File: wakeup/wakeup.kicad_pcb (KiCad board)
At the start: 2 copper layers, 12 parts, among them J1 Conn_01x03_Female, U1 74HC00, U2 74HC393

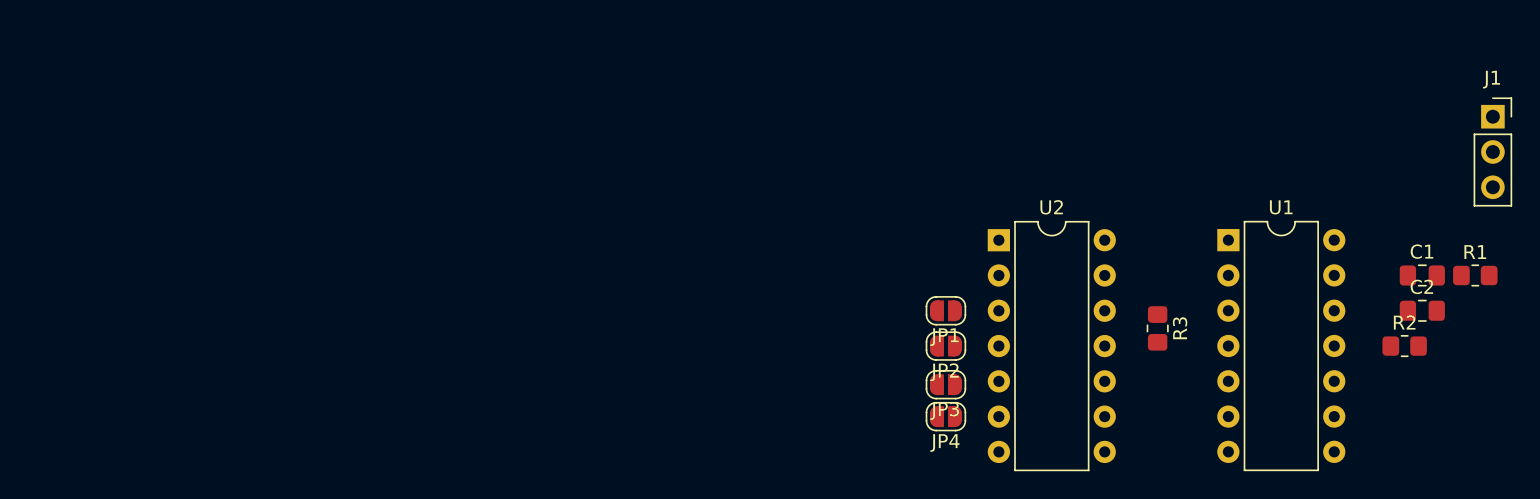
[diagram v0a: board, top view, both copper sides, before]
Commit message: Add power filter create pcb
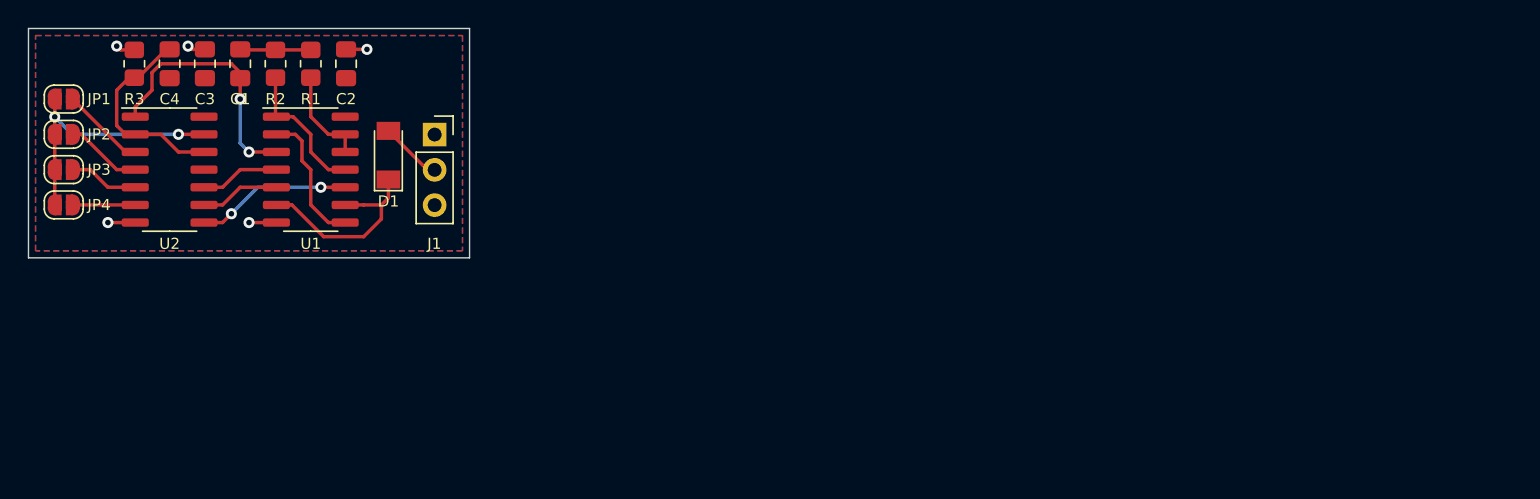
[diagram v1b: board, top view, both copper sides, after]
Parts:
- added C2: C, Capacitor_SMD:C_0805_2012Metric_Pad1.18x1.45mm_HandSolder, F.Cu at (48.3, 53.3)
- added C3: C, Capacitor_SMD:C_0805_2012Metric_Pad1.18x1.45mm_HandSolder, F.Cu at (38.1, 53.3)
- added D1: D, Diode_SMD:D_MiniMELF, F.Cu at (51.3, 59.9)
- U1, U2: footprint Package_DIP:DIP-14_W7.62mm -> Package_SO:SO-14_3.9x8.65mm_P1.27mm
- moved C4 91.9 mm to (35.6, 53.3), turned to 90 degrees
- moved C1 86.4 mm to (40.6, 53.3), turned to -90 degrees
- moved R1 85.2 mm to (45.7, 53.3), turned to -90 degrees
- moved R2 83.8 mm to (43.2, 53.3), turned to -90 degrees
- moved J1 76.2 mm to (54.6, 58.4)
- moved R3 76.1 mm to (33.0, 53.3), turned to 90 degrees
- moved U1 66.2 mm to (45.7, 61.0)
- moved JP3 65.4 mm to (27.9, 61.0)
- moved JP1 65.3 mm to (27.9, 55.9)
- moved JP2 65.3 mm to (27.9, 58.4)
- moved JP4 65.3 mm to (27.9, 63.5)
- moved U2 59.9 mm to (35.6, 61.0)
- renumbered C2 to C4
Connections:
- J1 pad 2: Net-(J1-Pad2) -> Net-(D1-Pad2)
- U1 pad 10: Net-(U1-Pad5) -> Net-(U1-Pad10)
- U1 pad 6: Net-(J1-Pad2) -> Net-(D1-Pad1)
- U1 pad 9: Net-(U2-Pad8) -> Net-(D1-Pad1)
- U2 pad 8: Net-(U2-Pad8) -> Net-(U1-Pad10)
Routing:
- net Net-(JP1-Pad2): track 0.00 -> 18.9 mm, vias 0 -> 2
- net Net-(C1-Pad2): track 0.00 -> 18.5 mm, vias 0 -> 2
- net Net-(D1-Pad1): track 0.00 -> 14.7 mm
- net Net-(C4-Pad2): track 0.00 -> 14.6 mm
- net Net-(U1-Pad10): track 0.00 -> 11.2 mm, vias 0 -> 2
- net Net-(R2-Pad2): track 0.00 -> 10.1 mm
- net Net-(U1-Pad2): track 0.00 -> 9.91 mm
- net GND: track 0.00 -> 8.14 mm, vias 0 -> 5
- net Net-(R1-Pad2): track 0.00 -> 7.08 mm
- net Net-(JP1-Pad1): track 0.00 -> 6.08 mm
- net Net-(U1-Pad5): track 0.00 -> 5.74 mm
- net Net-(U1-Pad4): track 0.00 -> 5.74 mm
- net Net-(JP2-Pad1): track 0.00 -> 5.55 mm
- net Net-(C1-Pad1): track 0.00 -> 5.10 mm
- net Net-(JP3-Pad1): track 0.00 -> 5.02 mm
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- added copper zone on B.Cu, net GND
- added copper zone on F.Cu, net VCC
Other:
- board outline added: 31.8 x 16.5 mm

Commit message: merge stage 1 update schematic ZX_keyboard
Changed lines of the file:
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@@
       (plotvalue true)
       (plotinvisibletext false)
-      (sketchpadsonfab false)
+      (sketchpadsonfab true)
       (subtractmaskfromsilk false)
       (outputformat 1)
       (mirror false)
-      (drillshape 1)
+      (drillshape 0)
       (scaleselection 1)
-      (outputdirectory "")
+      (outputdirectory "gerber/")
     )
   )
@@
     (fp_line (start -1 0.625) (end -1 -0.625) (layer "F.Fab") (width 0.1))
     (fp_line (start 1 -0.625) (end 1 0.625) (layer "F.Fab") (width 0.1))
-    (pad "1" smd roundrect (at -1.0375 0 90) (size 1.175 1.45) (layers "F.Cu" "F.Paste" "F.Mask") (roundrect_rratio 0.212766)
+    (pad "1" smd roundrect (at -1.0375 0 90) (size 1.175 1.45) (layers "F.Cu" "F.Paste" "F.Mask") (roundrect_rratio 0.2127659574)
       (net 3 "VCC") (pintype "passive"))
-    (pad "2" smd roundrect (at 1.0375 0 90) (size 1.175 1.45) (layers "F.Cu" "F.Paste" "F.Mask") (roundrect_rratio 0.212766)
+    (pad "2" smd roundrect (at 1.0375 0 90) (size 1.175 1.45) (layers "F.Cu" "F.Paste" "F.Mask") (roundrect_rratio 0.2127659574)
       (net 18 "Net-(C4-Pad2)") (pintype "passive"))
     (model "${KICAD6_3DMODEL_DIR}/Capacitor_SMD.3dshapes/C_0805_2012Metric.wrl"
@@
     (fp_line (start -1 0.625) (end -1 -0.625) (layer "F.Fab") (width 0.1))
     (fp_line (start 1 -0.625) (end 1 0.625) (layer "F.Fab") (width 0.1))
-    (pad "1" smd roundrect (at -1.0375 0 90) (size 1.175 1.45) (layers "F.Cu" "F.Paste" "F.Mask") (roundrect_rratio 0.212766)
+    (pad "1" smd roundrect (at -1.0375 0 90) (size 1.175 1.45) (layers "F.Cu" "F.Paste" "F.Mask") (roundrect_rratio 0.2127659574)
       (net 3 "VCC") (pintype "passive"))
-    (pad "2" smd roundrect (at 1.0375 0 90) (size 1.175 1.45) (layers "F.Cu" "F.Paste" "F.Mask") (roundrect_rratio 0.212766)
+    (pad "2" smd roundrect (at 1.0375 0 90) (size 1.175 1.45) (layers "F.Cu" "F.Paste" "F.Mask") (roundrect_rratio 0.2127659574)
       (net 4 "GND") (pintype "passive"))
     (model "${KICAD6_3DMODEL_DIR}/Capacitor_SMD.3dshapes/C_0805_2012Metric.wrl"
@@
     (fp_line (start 1 0.625) (end -1 0.625) (layer "F.Fab") (width 0.1))
     (fp_line (start -1 0.625) (end -1 -0.625) (layer "F.Fab") (width 0.1))
-    (pad "1" smd roundrect (at -1 0 90) (size 1.2 1.4) (layers "F.Cu" "F.Paste" "F.Mask") (roundrect_rratio 0.208333)
+    (pad "1" smd roundrect (at -1 0 90) (size 1.2 1.4) (layers "F.Cu" "F.Paste" "F.Mask") (roundrect_rratio 0.2083333333)
       (net 18 "Net-(C4-Pad2)") (pintype "passive"))
-    (pad "2" smd roundrect (at 1 0 90) (size 1.2 1.4) (layers "F.Cu" "F.Paste" "F.Mask") (roundrect_rratio 0.208333)
+    (pad "2" smd roundrect (at 1 0 90) (size 1.2 1.4) (layers "F.Cu" "F.Paste" "F.Mask") (roundrect_rratio 0.2083333333)
       (net 4 "GND") (pintype "passive"))
     (model "${KICAD6_3DMODEL_DIR}/Resistor_SMD.3dshapes/R_0805_2012Metric.wrl"
@@
     (fp_line (start 1 0.625) (end -1 0.625) (layer "F.Fab") (width 0.1))
     (fp_line (start 1 -0.625) (end 1 0.625) (layer "F.Fab") (width 0.1))
-    (pad "1" smd roundrect (at -1.0375 0 270) (size 1.175 1.45) (layers "F.Cu" "F.Paste" "F.Mask") (roundrect_rratio 0.212766)
+    (pad "1" smd roundrect (at -1.0375 0 270) (size 1.175 1.45) (layers "F.Cu" "F.Paste" "F.Mask") (roundrect_rratio 0.2127659574)
       (net 1 "Net-(C1-Pad1)") (pintype "passive"))
-    (pad "2" smd roundrect (at 1.0375 0 270) (size 1.175 1.45) (layers "F.Cu" "F.Paste" "F.Mask") (roundrect_rratio 0.212766)
+    (pad "2" smd roundrect (at 1.0375 0 270) (size 1.175 1.45) (layers "F.Cu" "F.Paste" "F.Mask") (roundrect_rratio 0.2127659574)
       (net 2 "Net-(C1-Pad2)") (pintype "passive"))
     (model "${KICAD6_3DMODEL_DIR}/Capacitor_SMD.3dshapes/C_0805_2012Metric.wrl"
@@
     (fp_line (start -1 -0.625) (end 1 -0.625) (layer "F.Fab") (width 0.1))
     (fp_line (start -1 0.625) (end -1 -0.625) (layer "F.Fab") (width 0.1))
-    (pad "1" smd roundrect (at -1.0375 0 90) (size 1.175 1.45) (layers "F.Cu" "F.Paste" "F.Mask") (roundrect_rratio 0.212766)
+    (pad "1" smd roundrect (at -1.0375 0 90) (size 1.175 1.45) (layers "F.Cu" "F.Paste" "F.Mask") (roundrect_rratio 0.2127659574)
       (net 3 "VCC") (pintype "passive"))
-    (pad "2" smd roundrect (at 1.0375 0 90) (size 1.175 1.45) (layers "F.Cu" "F.Paste" "F.Mask") (roundrect_rratio 0.212766)
+    (pad "2" smd roundrect (at 1.0375 0 90) (size 1.175 1.45) (layers "F.Cu" "F.Paste" "F.Mask") (roundrect_rratio 0.2127659574)
       (net 4 "GND") (pintype "passive"))
     (model "${KICAD6_3DMODEL_DIR}/Capacitor_SMD.3dshapes/C_0805_2012Metric.wrl"
@@
     (fp_line (start 1 0.625) (end -1 0.625) (layer "F.Fab") (width 0.1))
     (fp_line (start -1 -0.625) (end 1 -0.625) (layer "F.Fab") (width 0.1))
-    (pad "1" smd roundrect (at -1 0 270) (size 1.2 1.4) (layers "F.Cu" "F.Paste" "F.Mask") (roundrect_rratio 0.208333)
+    (pad "1" smd roundrect (at -1 0 270) (size 1.2 1.4) (layers "F.Cu" "F.Paste" "F.Mask") (roundrect_rratio 0.2083333333)
       (net 1 "Net-(C1-Pad1)") (pintype "passive"))
-    (pad "2" smd roundrect (at 1 0 270) (size 1.2 1.4) (layers "F.Cu" "F.Paste" "F.Mask") (roundrect_rratio 0.208333)
+    (pad "2" smd roundrect (at 1 0 270) (size 1.2 1.4) (layers "F.Cu" "F.Paste" "F.Mask") (roundrect_rratio 0.2083333333)
       (net 10 "Net-(R1-Pad2)") (pintype "passive"))
     (model "${KICAD6_3DMODEL_DIR}/Resistor_SMD.3dshapes/R_0805_2012Metric.wrl"
@@
     (fp_line (start -1 -0.625) (end 1 -0.625) (layer "F.Fab") (width 0.1))
     (fp_line (start 1 0.625) (end -1 0.625) (layer "F.Fab") (width 0.1))
-    (pad "1" smd roundrect (at -1 0 270) (size 1.2 1.4) (layers "F.Cu" "F.Paste" "F.Mask") (roundrect_rratio 0.208333)
+    (pad "1" smd roundrect (at -1 0 270) (size 1.2 1.4) (layers "F.Cu" "F.Paste" "F.Mask") (roundrect_rratio 0.2083333333)
       (net 1 "Net-(C1-Pad1)") (pintype "passive"))
-    (pad "2" smd roundrect (at 1 0 270) (size 1.2 1.4) (layers "F.Cu" "F.Paste" "F.Mask") (roundrect_rratio 0.208333)
+    (pad "2" smd roundrect (at 1 0 270) (size 1.2 1.4) (layers "F.Cu" "F.Paste" "F.Mask") (roundrect_rratio 0.2083333333)
       (net 11 "Net-(R2-Pad2)") (pintype "passive"))
     (model "${KICAD6_3DMODEL_DIR}/Resistor_SMD.3dshapes/R_0805_2012Metric.wrl"
